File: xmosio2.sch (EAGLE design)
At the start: 103 parts, among them IC1 IDTQS3245QSOP20, IC2 IDTQS3245QSOP20, IC3 IDTQS3245QSOP20, IC4 IDTQS3245QSOP20, IC5 IDTQS3245QSOP20, U1 24 MHz Osc. (F535L-24), U2 USD-SOCKETNEW, X1 0446200002

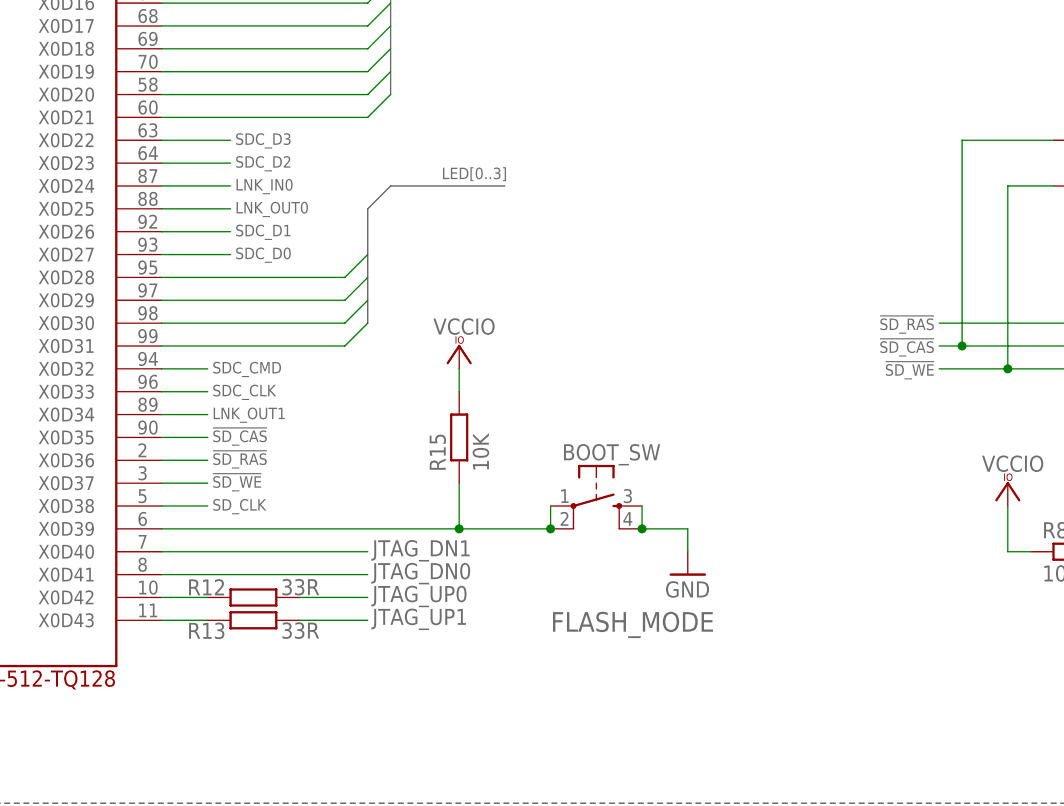
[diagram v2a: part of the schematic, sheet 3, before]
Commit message: - Add in zero-ohm resistor placeholders in case the drivers need 33R (like the JTAG interface does) - Better length matching, now sub-millimeter on all concerned traces - Move the boot-the-fallback-flash-image switch next to the reset switch - Move the decoupling capacitors closer to the XMOS chip - Move the SDRAM chip around to get better routing
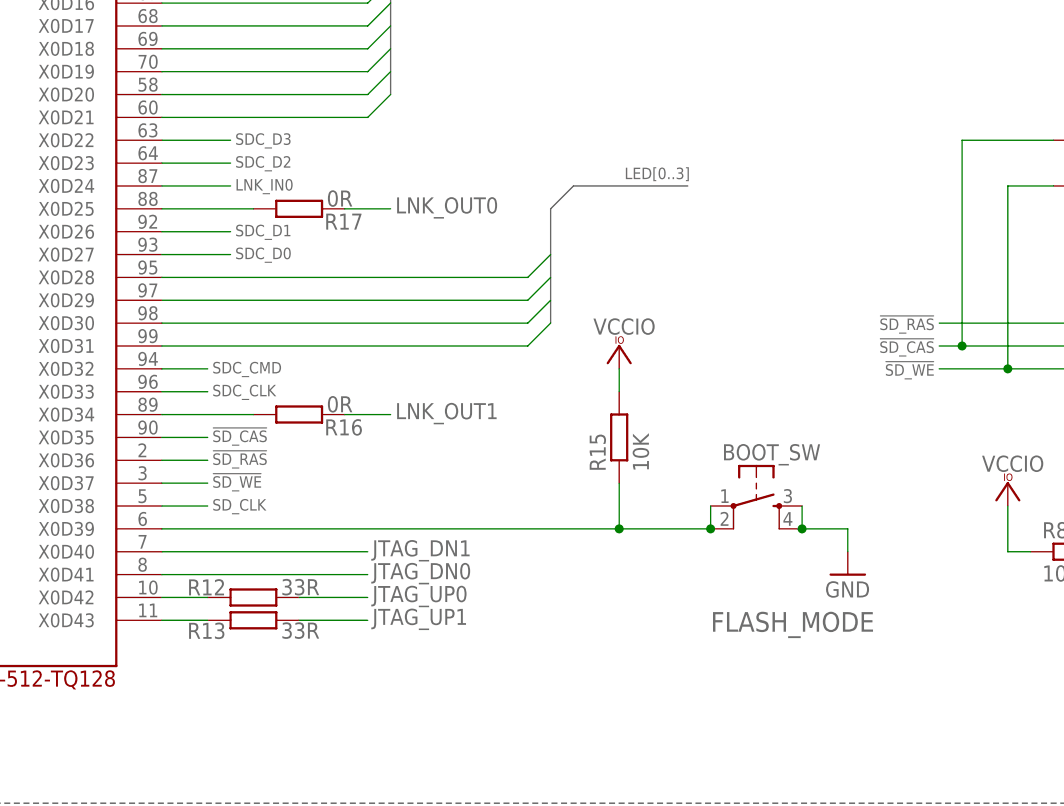
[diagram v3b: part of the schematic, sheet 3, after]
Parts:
- added R16, R17: 0R, rcl:R-EU_R0603
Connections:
- new net N$28: R17.1, U$2TILE0.X0D25@88
- new net N$29: R16.1, U$2TILE0.X0D34@89
- net LNK_OUT0: now also R17.2; no longer U$2TILE0.X0D25@88
- net LNK_OUT1: now also R16.2; no longer U$2TILE0.X0D34@89
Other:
- moved on the sheet: BOOT_SW, R15
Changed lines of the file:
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@@
 <setting verticaltext="up"/>
 </settings>
-<grid distance="0.1" unitdist="inch" unit="inch" style="lines" multiple="1" display="no" altdistance="0.01" altunitdist="inch" altunit="inch"/>
+<grid distance="0.1" unitdist="inch" unit="inch" style="lines" multiple="1" display="yes" altdistance="0.01" altunitdist="inch" altunit="inch"/>
 <layers>
 <layer number="1" name="Top" color="4" fill="1" visible="no" active="no"/>
@@
 <part name="R15" library="rcl" deviceset="R-EU_" device="R0603" value="10K"/>
 <part name="VCC25" library="supply1" deviceset="VCCIO" device=""/>
+<part name="R16" library="rcl" deviceset="R-EU_" device="R0603" value="0R"/>
+<part name="R17" library="rcl" deviceset="R-EU_" device="R0603" value="0R"/>
 </parts>
 <sheets>
@@
 </instance>
 <instance part="FRAME3" gate="G$1" x="-58.42" y="-129.54"/>
-<instance part="BOOT_SW" gate="S" x="35.56" y="-5.08" smashed="yes">
-<attribute name="NAME" x="31.75" y="0" size="1.778" layer="95"/>
-<attribute name="VALUE" x="30.48" y="-19.05" size="2.1844" layer="96"/>
-</instance>
-<instance part="GND38" gate="1" x="45.72" y="-12.7"/>
-<instance part="R15" gate="G$1" x="20.32" y="2.54" rot="R90"/>
-<instance part="VCC25" gate="G$1" x="20.32" y="12.7" smashed="yes">
-<attribute name="VALUE" x="24.384" y="15.748" size="1.778" layer="96" rot="R180"/>
+<instance part="BOOT_SW" gate="S" x="53.34" y="-5.08" smashed="yes">
+<attribute name="NAME" x="49.53" y="0" size="1.778" layer="95"/>
+<attribute name="VALUE" x="48.26" y="-19.05" size="2.1844" layer="96"/>
+</instance>
+<instance part="GND38" gate="1" x="63.5" y="-12.7"/>
+<instance part="R15" gate="G$1" x="38.1" y="2.54" rot="R90"/>
+<instance part="VCC25" gate="G$1" x="38.1" y="12.7" smashed="yes">
+<attribute name="VALUE" x="42.164" y="15.748" size="1.778" layer="96" rot="R180"/>
+</instance>
+<instance part="R16" gate="G$1" x="2.54" y="5.08" smashed="yes">
+<attribute name="NAME" x="5.334" y="2.7686" size="1.778" layer="95"/>
+<attribute name="VALUE" x="5.588" y="5.334" size="1.778" layer="96"/>
+</instance>
+<instance part="R17" gate="G$1" x="2.54" y="27.94" smashed="yes">
+<attribute name="NAME" x="5.334" y="25.6286" size="1.778" layer="95"/>
+<attribute name="VALUE" x="5.588" y="28.194" size="1.778" layer="96"/>
 </instance>
 </instances>
@@
 <bus name="LED[0..3]">
 <segment>
-<wire x1="10.16" y1="15.24" x2="10.16" y2="27.94" width="0.762" layer="92"/>
-<wire x1="10.16" y1="27.94" x2="12.7" y2="30.48" width="0.762" layer="92"/>
-<wire x1="12.7" y1="30.48" x2="25.4" y2="30.48" width="0.762" layer="92"/>
-<label x="25.654" y="32.512" size="1.27" layer="95" rot="R180"/>
+<wire x1="30.48" y1="15.24" x2="30.48" y2="27.94" width="0.762" layer="92"/>
+<wire x1="30.48" y1="27.94" x2="33.02" y2="30.48" width="0.762" layer="92"/>
+<wire x1="33.02" y1="30.48" x2="45.72" y2="30.48" width="0.762" layer="92"/>
+<label x="45.974" y="32.512" size="1.27" layer="95" rot="R180"/>
 </segment>
 </bus>
@@
 <pinref part="R15" gate="G$1" pin="2"/>
 <pinref part="VCC25" gate="G$1" pin="VCCIO"/>
-<wire x1="20.32" y1="7.62" x2="20.32" y2="10.16" width="0.1524" layer="91"/>
+<wire x1="38.1" y1="7.62" x2="38.1" y2="10.16" width="0.1524" layer="91"/>
 </segment>
 </net>
@@
 <pinref part="BOOT_SW" gate="S" pin="3"/>
 <pinref part="BOOT_SW" gate="S" pin="4"/>
-<wire x1="40.64" y1="-5.08" x2="40.64" y2="-7.62" width="0.1524" layer="91"/>
+<wire x1="58.42" y1="-5.08" x2="58.42" y2="-7.62" width="0.1524" layer="91"/>
 <pinref part="GND38" gate="1" pin="GND"/>
-<wire x1="40.64" y1="-7.62" x2="45.72" y2="-7.62" width="0.1524" layer="91"/>
-<wire x1="45.72" y1="-7.62" x2="45.72" y2="-10.16" width="0.1524" layer="91"/>
-<junction x="40.64" y="-7.62"/>
+<wire x1="58.42" y1="-7.62" x2="63.5" y2="-7.62" width="0.1524" layer="91"/>
+<wire x1="63.5" y1="-7.62" x2="63.5" y2="-10.16" width="0.1524" layer="91"/>
+<junction x="58.42" y="-7.62"/>
 </segment>
 </net>
@@
 <net name="LNK_OUT0" class="0">
 <segment>
-<pinref part="U$2" gate="TILE0" pin="X0D25@88"/>
-<wire x1="-12.7" y1="27.94" x2="-5.08" y2="27.94" width="0.1524" layer="91"/>
-<label x="-4.572" y="27.432" size="1.27" layer="95"/>
+<pinref part="R17" gate="G$1" pin="2"/>
+<wire x1="7.62" y1="27.94" x2="12.7" y2="27.94" width="0.1524" layer="91"/>
+<label x="13.208" y="27.432" size="1.778" layer="95"/>
 </segment>
 </net>
 <net name="LNK_OUT1" class="0">
 <segment>
-<pinref part="U$2" gate="TILE0" pin="X0D34@89"/>
-<wire x1="-12.7" y1="5.08" x2="-7.62" y2="5.08" width="0.1524" layer="91"/>
-<label x="-7.112" y="4.572" size="1.27" layer="95"/>
+<pinref part="R16" gate="G$1" pin="2"/>
+<wire x1="7.62" y1="5.08" x2="12.7" y2="5.08" width="0.1524" layer="91"/>
+<label x="13.208" y="4.572" size="1.778" layer="95"/>
 </segment>
 </net>
@@
 <segment>
 <pinref part="U$2" gate="TILE0" pin="X0D31@99"/>
-<wire x1="10.16" y1="15.24" x2="7.62" y2="12.7" width="0.1524" layer="91"/>
-<wire x1="7.62" y1="12.7" x2="-12.7" y2="12.7" width="0.1524" layer="91"/>
+<wire x1="30.48" y1="15.24" x2="27.94" y2="12.7" width="0.1524" layer="91"/>
+<wire x1="27.94" y1="12.7" x2="-12.7" y2="12.7" width="0.1524" layer="91"/>
 </segment>
 </net>
@@
 <segment>
 <pinref part="U$2" gate="TILE0" pin="X0D30@98"/>
-<wire x1="10.16" y1="17.78" x2="7.62" y2="15.24" width="0.1524" layer="91"/>
-<wire x1="7.62" y1="15.24" x2="-12.7" y2="15.24" width="0.1524" layer="91"/>
+<wire x1="30.48" y1="17.78" x2="27.94" y2="15.24" width="0.1524" layer="91"/>
+<wire x1="27.94" y1="15.24" x2="-12.7" y2="15.24" width="0.1524" layer="91"/>
 </segment>
 </net>
@@
 <segment>
 <pinref part="U$2" gate="TILE0" pin="X0D29@97"/>
-<wire x1="10.16" y1="20.32" x2="7.62" y2="17.78" width="0.1524" layer="91"/>
-<wire x1="7.62" y1="17.78" x2="-12.7" y2="17.78" width="0.1524" layer="91"/>
+<wire x1="30.48" y1="20.32" x2="27.94" y2="17.78" width="0.1524" layer="91"/>
+<wire x1="27.94" y1="17.78" x2="-12.7" y2="17.78" width="0.1524" layer="91"/>
 </segment>
 </net>
@@
 <segment>
 <pinref part="U$2" gate="TILE0" pin="X0D28@95"/>
-<wire x1="10.16" y1="22.86" x2="7.62" y2="20.32" width="0.1524" layer="91"/>
-<wire x1="7.62" y1="20.32" x2="-12.7" y2="20.32" width="0.1524" layer="91"/>
+<wire x1="30.48" y1="22.86" x2="27.94" y2="20.32" width="0.1524" layer="91"/>
+<wire x1="27.94" y1="20.32" x2="-12.7" y2="20.32" width="0.1524" layer="91"/>
 </segment>
 </net>
@@
 <pinref part="U$2" gate="TILE0" pin="X0D39@6"/>
 <pinref part="BOOT_SW" gate="S" pin="2"/>
-<wire x1="30.48" y1="-7.62" x2="20.32" y2="-7.62" width="0.1524" layer="91"/>
+<wire x1="48.26" y1="-7.62" x2="38.1" y2="-7.62" width="0.1524" layer="91"/>
 <pinref part="BOOT_SW" gate="S" pin="1"/>
-<wire x1="20.32" y1="-7.62" x2="-12.7" y2="-7.62" width="0.1524" layer="91"/>
-<wire x1="30.48" y1="-7.62" x2="30.48" y2="-5.08" width="0.1524" layer="91"/>
-<junction x="30.48" y="-7.62"/>
+<wire x1="38.1" y1="-7.62" x2="-12.7" y2="-7.62" width="0.1524" layer="91"/>
+<wire x1="48.26" y1="-7.62" x2="48.26" y2="-5.08" width="0.1524" layer="91"/>
+<junction x="48.26" y="-7.62"/>
 <pinref part="R15" gate="G$1" pin="1"/>
-<wire x1="20.32" y1="-2.54" x2="20.32" y2="-7.62" width="0.1524" layer="91"/>
-<junction x="20.32" y="-7.62"/>
+<wire x1="38.1" y1="-2.54" x2="38.1" y2="-7.62" width="0.1524" layer="91"/>
+<junction x="38.1" y="-7.62"/>
 </segment>
 </net>
@@
 </segment>
 </net>
+<net name="N$28" class="0">
+<segment>
+<pinref part="U$2" gate="TILE0" pin="X0D25@88"/>
+<pinref part="R17" gate="G$1" pin="1"/>
+<wire x1="-12.7" y1="27.94" x2="-2.54" y2="27.94" width="0.1524" layer="91"/>
+</segment>
+</net>
+<net name="N$29" class="0">
+<segment>
+<pinref part="U$2" gate="TILE0" pin="X0D34@89"/>
+<pinref part="R16" gate="G$1" pin="1"/>
+<wire x1="-12.7" y1="5.08" x2="-2.54" y2="5.08" width="0.1524" layer="91"/>
+</segment>
+</net>

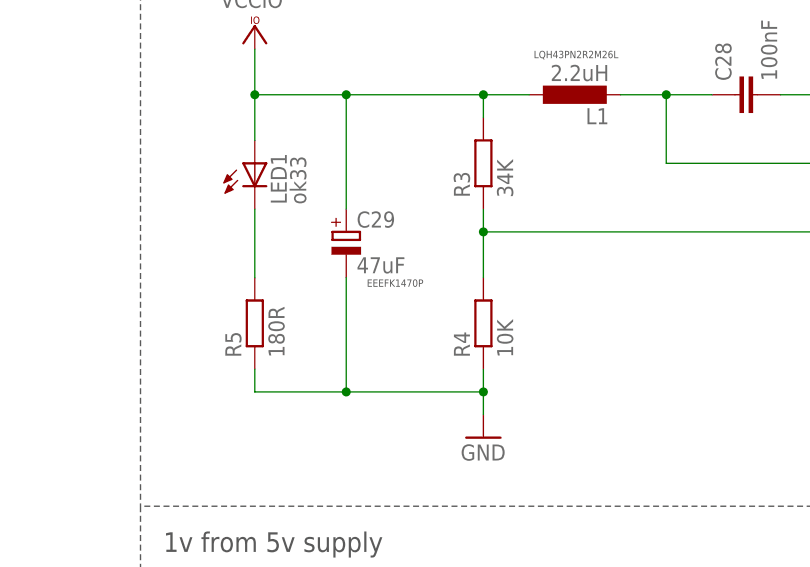
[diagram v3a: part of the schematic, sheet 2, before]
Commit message: - Add some keepouts for easier soldering - Change the 0805 capacitors to be 0603
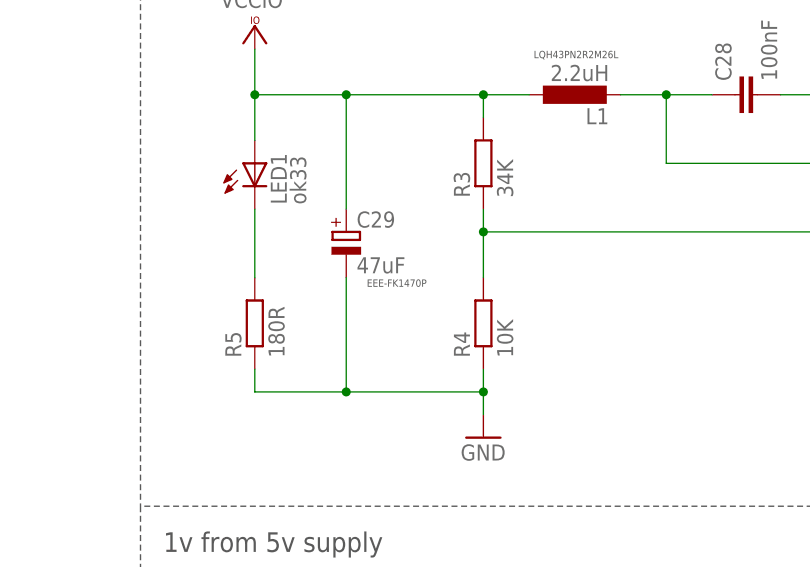
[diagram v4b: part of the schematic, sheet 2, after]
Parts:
- C1, C2, C3, C4, C5: device rcl:C-EUC0805 -> rcl:C-EUC0603
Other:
- note added: "EEE-FK1470P"
- note added: "W9825G6KH"
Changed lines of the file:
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@@
 <grid distance="0.1" unitdist="inch" unit="inch" style="lines" multiple="1" display="yes" altdistance="0.01" altunitdist="inch" altunit="inch"/>
 <layers>
-<layer number="1" name="Top" color="4" fill="1" visible="no" active="no"/>
-<layer number="2" name="Route2" color="1" fill="3" visible="no" active="no"/>
-<layer number="3" name="Route3" color="4" fill="3" visible="no" active="no"/>
-<layer number="14" name="Route14" color="1" fill="6" visible="no" active="no"/>
-<layer number="15" name="Route15" color="4" fill="6" visible="no" active="no"/>
-<layer number="16" name="Bottom" color="1" fill="1" visible="no" active="no"/>
-<layer number="17" name="Pads" color="2" fill="1" visible="no" active="no"/>
-<layer number="18" name="Vias" color="2" fill="1" visible="no" active="no"/>
-<layer number="19" name="Unrouted" color="6" fill="1" visible="no" active="no"/>
-<layer number="20" name="Dimension" color="15" fill="1" visible="no" active="no"/>
-<layer number="21" name="tPlace" color="7" fill="1" visible="no" active="no"/>
-<layer number="22" name="bPlace" color="7" fill="1" visible="no" active="no"/>
-<layer number="23" name="tOrigins" color="15" fill="1" visible="no" active="no"/>
-<layer number="24" name="bOrigins" color="15" fill="1" visible="no" active="no"/>
-<layer number="25" name="tNames" color="7" fill="1" visible="no" active="no"/>
-<layer number="26" name="bNames" color="7" fill="1" visible="no" active="no"/>
-<layer number="27" name="tValues" color="7" fill="1" visible="no" active="no"/>
-<layer number="28" name="bValues" color="7" fill="1" visible="no" active="no"/>
+<layer number="1" name="Top" color="4" fill="1" visible="yes" active="no"/>
+<layer number="2" name="Route2" color="1" fill="3" visible="yes" active="no"/>
+<layer number="3" name="Route3" color="4" fill="3" visible="yes" active="no"/>
+<layer number="14" name="Route14" color="1" fill="6" visible="yes" active="no"/>
+<layer number="15" name="Route15" color="4" fill="6" visible="yes" active="no"/>
+<layer number="16" name="Bottom" color="1" fill="1" visible="yes" active="no"/>
+<layer number="17" name="Pads" color="2" fill="1" visible="yes" active="no"/>
+<layer number="18" name="Vias" color="2" fill="1" visible="yes" active="no"/>
+<layer number="19" name="Unrouted" color="6" fill="1" visible="yes" active="no"/>
+<layer number="20" name="Dimension" color="15" fill="1" visible="yes" active="no"/>
+<layer number="21" name="tPlace" color="7" fill="1" visible="yes" active="no"/>
+<layer number="22" name="bPlace" color="7" fill="1" visible="yes" active="no"/>
+<layer number="23" name="tOrigins" color="15" fill="1" visible="yes" active="no"/>
+<layer number="24" name="bOrigins" color="15" fill="1" visible="yes" active="no"/>
+<layer number="25" name="tNames" color="7" fill="1" visible="yes" active="no"/>
+<layer number="26" name="bNames" color="7" fill="1" visible="yes" active="no"/>
+<layer number="27" name="tValues" color="7" fill="1" visible="yes" active="no"/>
+<layer number="28" name="bValues" color="7" fill="1" visible="yes" active="no"/>
 <layer number="29" name="tStop" color="7" fill="3" visible="no" active="no"/>
 <layer number="30" name="bStop" color="7" fill="6" visible="no" active="no"/>
@@
 <layer number="35" name="tGlue" color="7" fill="4" visible="no" active="no"/>
 <layer number="36" name="bGlue" color="7" fill="5" visible="no" active="no"/>
-<layer number="37" name="tTest" color="7" fill="1" visible="no" active="no"/>
-<layer number="38" name="bTest" color="7" fill="1" visible="no" active="no"/>
+<layer number="37" name="tTest" color="7" fill="1" visible="yes" active="no"/>
+<layer number="38" name="bTest" color="7" fill="1" visible="yes" active="no"/>
 <layer number="39" name="tKeepout" color="4" fill="11" visible="no" active="no"/>
 <layer number="40" name="bKeepout" color="1" fill="11" visible="no" active="no"/>
@@
 <layer number="44" name="Drills" color="7" fill="1" visible="no" active="no"/>
 <layer number="45" name="Holes" color="7" fill="1" visible="no" active="no"/>
-<layer number="46" name="Milling" color="3" fill="1" visible="no" active="no"/>
-<layer number="47" name="Measures" color="7" fill="1" visible="no" active="no"/>
-<layer number="48" name="Document" color="7" fill="1" visible="no" active="no"/>
-<layer number="49" name="Reference" color="7" fill="1" visible="no" active="no"/>
-<layer number="50" name="dxf" color="7" fill="1" visible="no" active="no"/>
-<layer number="51" name="tDocu" color="7" fill="1" visible="no" active="no"/>
-<layer number="52" name="bDocu" color="7" fill="1" visible="no" active="no"/>
-<layer number="53" name="tGND_GNDA" color="7" fill="9" visible="no" active="no"/>
-<layer number="54" name="bGND_GNDA" color="1" fill="9" visible="no" active="no"/>
-<layer number="56" name="wert" color="7" fill="1" visible="no" active="no"/>
-<layer number="57" name="tCAD" color="7" fill="1" visible="no" active="no"/>
+<layer number="46" name="Milling" color="3" fill="1" visible="yes" active="no"/>
+<layer number="47" name="Measures" color="7" fill="1" visible="yes" active="no"/>
+<layer number="48" name="Document" color="7" fill="1" visible="yes" active="no"/>
+<layer number="49" name="Reference" color="7" fill="1" visible="yes" active="no"/>
+<layer number="50" name="dxf" color="7" fill="1" visible="yes" active="no"/>
+<layer number="51" name="tDocu" color="7" fill="1" visible="yes" active="no"/>
+<layer number="52" name="bDocu" color="7" fill="1" visible="yes" active="no"/>
+<layer number="53" name="tGND_GNDA" color="7" fill="9" visible="yes" active="no"/>
+<layer number="54" name="bGND_GNDA" color="1" fill="9" visible="yes" active="no"/>
+<layer number="56" name="wert" color="7" fill="1" visible="yes" active="no"/>
+<layer number="57" name="tCAD" color="7" fill="1" visible="yes" active="no"/>
 <layer number="90" name="Modules" color="5" fill="1" visible="yes" active="yes"/>
 <layer number="91" name="Nets" color="2" fill="1" visible="yes" active="yes"/>
@@
 <part name="IC5" library="IDTQS_3245QG" deviceset="IDTQS3245" device="QSOP20"/>
 <part name="GND11" library="supply1" deviceset="GND" device=""/>
-<part name="C5" library="rcl" deviceset="C-EU" device="C0805" value="100nF"/>
+<part name="C5" library="rcl" deviceset="C-EU" device="C0603" value="100nF"/>
 <part name="GND1" library="supply1" deviceset="GND" device=""/>
-<part name="C1" library="rcl" deviceset="C-EU" device="C0805" value="100nF"/>
+<part name="C1" library="rcl" deviceset="C-EU" device="C0603" value="100nF"/>
 <part name="GND2" library="supply1" deviceset="GND" device=""/>
-<part name="C2" library="rcl" deviceset="C-EU" device="C0805" value="100nF"/>
+<part name="C2" library="rcl" deviceset="C-EU" device="C0603" value="100nF"/>
 <part name="GND3" library="supply1" deviceset="GND" device=""/>
-<part name="C3" library="rcl" deviceset="C-EU" device="C0805" value="100nF"/>
+<part name="C3" library="rcl" deviceset="C-EU" device="C0603" value="100nF"/>
 <part name="GND4" library="supply1" deviceset="GND" device=""/>
-<part name="C4" library="rcl" deviceset="C-EU" device="C0805" value="100nF"/>
+<part name="C4" library="rcl" deviceset="C-EU" device="C0603" value="100nF"/>
 <part name="GND5" library="supply1" deviceset="GND" device=""/>
 <part name="GND6" library="supply1" deviceset="GND" device=""/>
@@
 <text x="281.432" y="51.816" size="0.8128" layer="97">EEEFK1V220R</text>
 <text x="198.628" y="67.564" size="0.8128" layer="97">LQH43PN2R2M26L</text>
-<text x="180.086" y="42.164" size="0.8128" layer="97">EEEFK1470P</text>
+<text x="180.086" y="42.164" size="0.8128" layer="97">EEE-FK1470P</text>
 <wire x1="154.94" y1="86.36" x2="154.94" y2="17.78" width="0.1524" layer="97" style="shortdash"/>
 <wire x1="314.96" y1="17.78" x2="314.96" y2="86.36" width="0.1524" layer="97" style="shortdash"/>
@@
 <text x="170.18" y="-43.18" size="2.1844" layer="97">Note: PCB is arranged so that the MUX does not interfere with the signal trace length to any significant extent</text>
 <text x="170.18" y="-38.1" size="2.1844" layer="97">Note: SDRAM byte lanes aren't supported. Do a read/modify/write to write individual bytes </text>
+<text x="127" y="-22.86" size="1.778" layer="97">W9825G6KH</text>
 </plain>
 <instances>
